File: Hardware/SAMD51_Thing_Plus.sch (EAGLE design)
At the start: 51 parts, among them J6 AMP FCI 10103594-0001LF, Q1 2.5A/30V, U1 MCP73831, U2 ATSAMD51J20A-A, U3 AP2112K-3.3V, U4 4MB Flash, Y1 32.768kHz

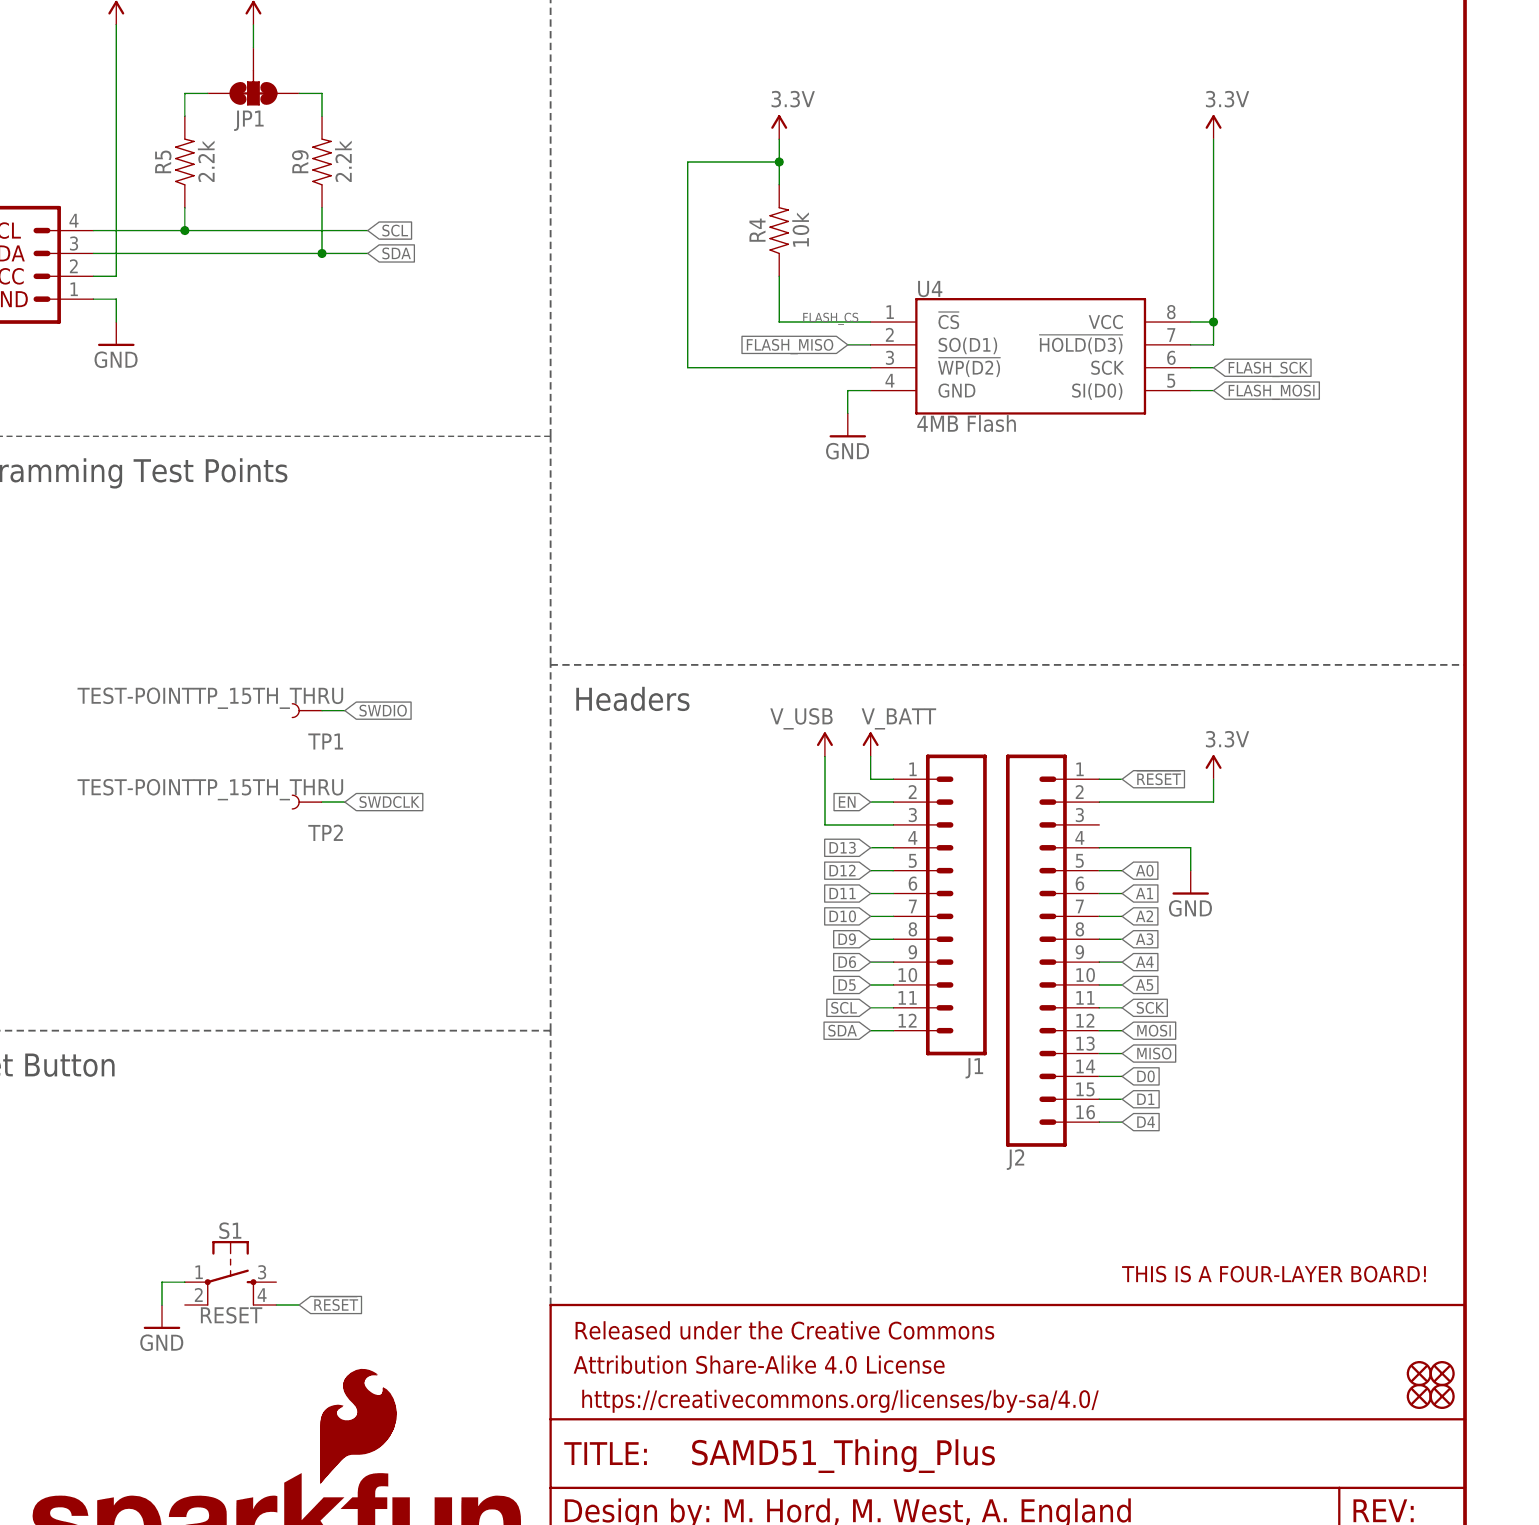
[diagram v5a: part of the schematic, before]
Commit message: adding i2c labels from double check
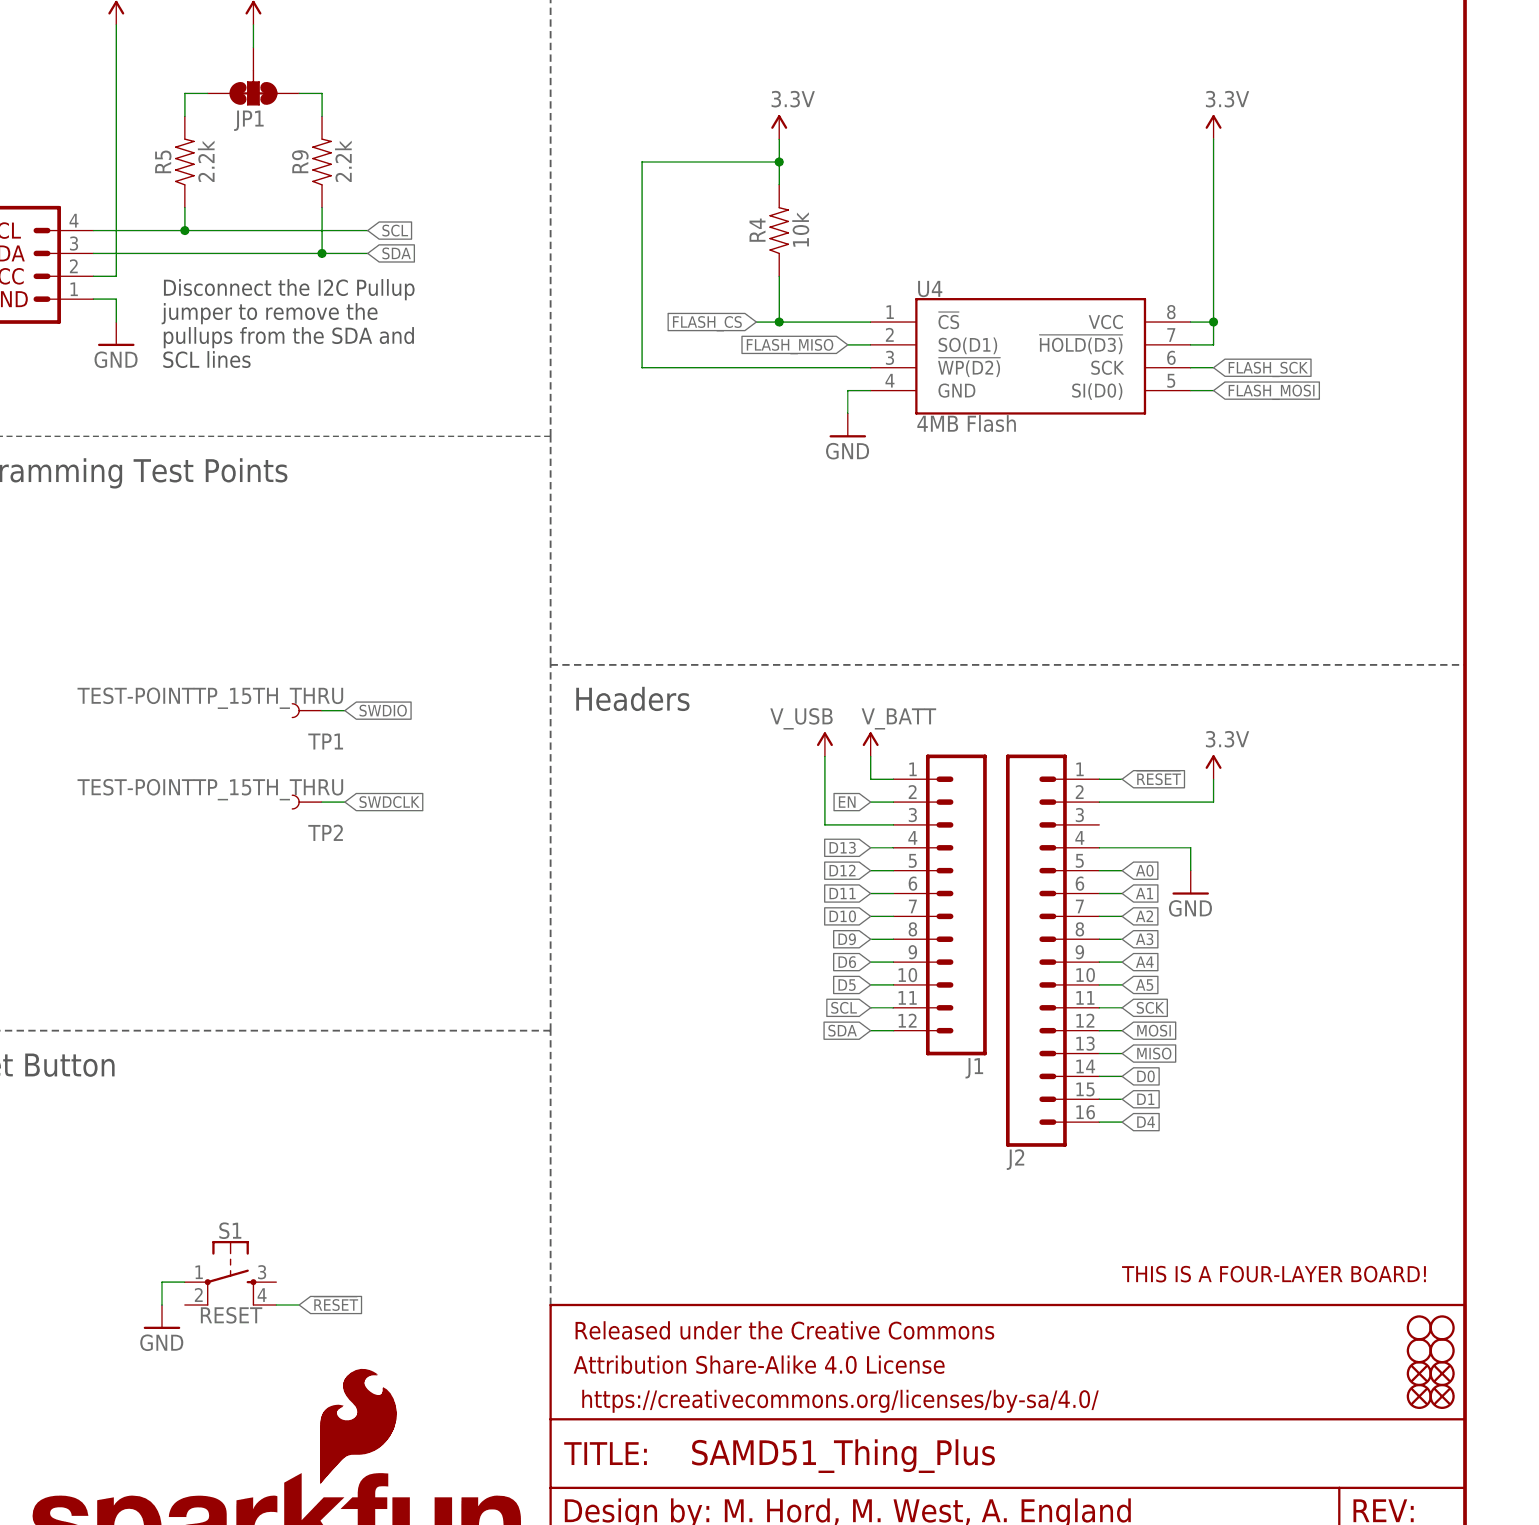
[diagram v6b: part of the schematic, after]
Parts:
- added H1, H2, H3, H4: STAND-OFF, SparkFun-Hardware:STAND-OFF
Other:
- note added: "Disconnect the I2C Pullup jumper to remove the pullups from the SDA and SCL lines"
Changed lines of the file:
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@@
 <part name="JP1" library="SparkFun-Jumpers" deviceset="JUMPER-SMT_3_2-NC_TRACE" device="_SILK"/>
 <part name="SUPPLY15" library="SparkFun-Aesthetics" deviceset="3.3V" device=""/>
+<part name="H1" library="SparkFun-Hardware" deviceset="STAND-OFF" device=""/>
+<part name="H2" library="SparkFun-Hardware" deviceset="STAND-OFF" device=""/>
+<part name="H3" library="SparkFun-Hardware" deviceset="STAND-OFF" device=""/>
+<part name="H4" library="SparkFun-Hardware" deviceset="STAND-OFF" device=""/>
 </parts>
 <sheets>
@@
 <text x="332.74" y="187.96" size="2.54" layer="97" font="vector">Flash Memory</text>
 <wire x1="129.54" y1="193.04" x2="259.08" y2="193.04" width="0.1524" layer="97" style="longdash"/>
+<text x="287.02" y="139.7" size="1.778" layer="97" font="vector">Disconnect the I2C Pullup
+jumper to remove the
+pullups from the SDA and
+SCL lines</text>
 </plain>
 <instances>
@@
 </instance>
 <instance part="SUPPLY15" gate="G$1" x="297.18" y="177.8"/>
+<instance part="H1" gate="G$1" x="426.72" y="30.48"/>
+<instance part="H2" gate="G$1" x="426.72" y="33.02"/>
+<instance part="H3" gate="G$1" x="429.26" y="33.02"/>
+<instance part="H4" gate="G$1" x="429.26" y="30.48"/>
 </instances>
 <busses>
@@
 <pinref part="U4" gate="G$1" pin="!WP(D2)"/>
 <wire x1="355.6" y1="162.56" x2="355.6" y2="165.1" width="0.1524" layer="91"/>
-<wire x1="365.76" y1="139.7" x2="345.44" y2="139.7" width="0.1524" layer="91"/>
-<wire x1="345.44" y1="139.7" x2="345.44" y2="162.56" width="0.1524" layer="91"/>
-<wire x1="345.44" y1="162.56" x2="355.6" y2="162.56" width="0.1524" layer="91"/>
+<wire x1="365.76" y1="139.7" x2="340.36" y2="139.7" width="0.1524" layer="91"/>
+<wire x1="340.36" y1="139.7" x2="340.36" y2="162.56" width="0.1524" layer="91"/>
+<wire x1="340.36" y1="162.56" x2="355.6" y2="162.56" width="0.1524" layer="91"/>
 <junction x="355.6" y="162.56"/>
 </segment>
@@
 <wire x1="355.6" y1="144.78" x2="355.6" y2="149.86" width="0.1524" layer="91"/>
 <pinref part="R4" gate="G$1" pin="1"/>
-<label x="358.14" y="144.78" size="1.016" layer="95" font="vector"/>
-</segment>
-<segment>
+<label x="353.06" y="144.78" size="1.27" layer="95" font="vector" rot="R180" xref="yes"/>
+<wire x1="355.6" y1="144.78" x2="353.06" y2="144.78" width="0.1524" layer="91"/>
+<junction x="355.6" y="144.78"/>
+</segment>
+<segment>

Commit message: pre-design review changes
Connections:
- net D1: now also U2.PA12; no longer U2.PA14
- net FLASH_MOSI: now also U2.PA08; no longer U2.PA09
- net FLASH_SCK: now also U2.PA09; no longer U2.PA08
- net SCK: now also U2.PB13; no longer U2.PA12
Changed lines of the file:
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@@
 </segment>
 <segment>
-<pinref part="U2" gate="G$1" pin="PA08"/>
-<wire x1="93.98" y1="124.46" x2="91.44" y2="124.46" width="0.1524" layer="91"/>
-<label x="91.44" y="124.46" size="1.27" layer="95" font="vector" rot="R180" xref="yes"/>
+<pinref part="U2" gate="G$1" pin="PA09"/>
+<wire x1="93.98" y1="121.92" x2="91.44" y2="121.92" width="0.1524" layer="91"/>
+<label x="91.44" y="121.92" size="1.27" layer="95" font="vector" rot="R180" xref="yes"/>
 </segment>
 </net>
@@
 </segment>
 <segment>
-<pinref part="U2" gate="G$1" pin="PA09"/>
-<wire x1="93.98" y1="121.92" x2="91.44" y2="121.92" width="0.1524" layer="91"/>
-<label x="91.44" y="121.92" size="1.27" layer="95" font="vector" rot="R180" xref="yes"/>
+<pinref part="U2" gate="G$1" pin="PA08"/>
+<wire x1="93.98" y1="124.46" x2="91.44" y2="124.46" width="0.1524" layer="91"/>
+<label x="91.44" y="124.46" size="1.27" layer="95" font="vector" rot="R180" xref="yes"/>
 </segment>
 </net>
@@
 </segment>
 <segment>
+<pinref part="U2" gate="G$1" pin="PB13"/>
+<wire x1="152.4" y1="111.76" x2="154.94" y2="111.76" width="0.1524" layer="91"/>
+<label x="154.94" y="111.76" size="1.27" layer="95" xref="yes"/>
+</segment>
+</net>
+<net name="MOSI" class="0">
+<segment>
+<pinref part="J2" gate="G$1" pin="12"/>
+<wire x1="391.16" y1="66.04" x2="393.7" y2="66.04" width="0.1524" layer="91"/>
+<label x="393.7" y="66.04" size="1.27" layer="95" font="vector" xref="yes"/>
+</segment>
+<segment>
+<pinref part="U2" gate="G$1" pin="PB12"/>
+<wire x1="152.4" y1="114.3" x2="154.94" y2="114.3" width="0.1524" layer="91"/>
+<label x="154.94" y="114.3" size="1.27" layer="95" font="vector" xref="yes"/>
+</segment>
+</net>
+<net name="MISO" class="0">
+<segment>
+<pinref part="J2" gate="G$1" pin="13"/>
+<wire x1="391.16" y1="63.5" x2="393.7" y2="63.5" width="0.1524" layer="91"/>
+<label x="393.7" y="63.5" size="1.27" layer="95" font="vector" xref="yes"/>
+</segment>
+<segment>
+<pinref part="U2" gate="G$1" pin="PB11"/>
+<wire x1="152.4" y1="116.84" x2="154.94" y2="116.84" width="0.1524" layer="91"/>
+<label x="154.94" y="116.84" size="1.27" layer="95" font="vector" xref="yes"/>
+</segment>
+</net>
+<net name="D0" class="0">
+<segment>
+<pinref part="J2" gate="G$1" pin="14"/>
+<wire x1="391.16" y1="60.96" x2="393.7" y2="60.96" width="0.1524" layer="91"/>
+<label x="393.7" y="60.96" size="1.27" layer="95" font="vector" xref="yes"/>
+</segment>
+<segment>
+<pinref part="U2" gate="G$1" pin="PA13"/>
+<wire x1="93.98" y1="111.76" x2="91.44" y2="111.76" width="0.1524" layer="91"/>
+<label x="91.44" y="111.76" size="1.27" layer="95" font="vector" rot="R180" xref="yes"/>
+</segment>
+</net>
+<net name="D1" class="0">
+<segment>
+<pinref part="J2" gate="G$1" pin="15"/>
+<wire x1="391.16" y1="58.42" x2="393.7" y2="58.42" width="0.1524" layer="91"/>
+<label x="393.7" y="58.42" size="1.27" layer="95" font="vector" xref="yes"/>
+</segment>
+<segment>
 <pinref part="U2" gate="G$1" pin="PA12"/>
 <wire x1="93.98" y1="114.3" x2="91.44" y2="114.3" width="0.1524" layer="91"/>
@@
 </segment>
 </net>
-<net name="MOSI" class="0">
-<segment>
-<pinref part="J2" gate="G$1" pin="12"/>
-<wire x1="391.16" y1="66.04" x2="393.7" y2="66.04" width="0.1524" layer="91"/>
-<label x="393.7" y="66.04" size="1.27" layer="95" font="vector" xref="yes"/>
-</segment>
-<segment>
-<pinref part="U2" gate="G$1" pin="PB12"/>
-<wire x1="152.4" y1="114.3" x2="154.94" y2="114.3" width="0.1524" layer="91"/>
-<label x="154.94" y="114.3" size="1.27" layer="95" font="vector" xref="yes"/>
-</segment>
-</net>
-<net name="MISO" class="0">
-<segment>
-<pinref part="J2" gate="G$1" pin="13"/>
-<wire x1="391.16" y1="63.5" x2="393.7" y2="63.5" width="0.1524" layer="91"/>
-<label x="393.7" y="63.5" size="1.27" layer="95" font="vector" xref="yes"/>
-</segment>
-<segment>
-<pinref part="U2" gate="G$1" pin="PB11"/>
-<wire x1="152.4" y1="116.84" x2="154.94" y2="116.84" width="0.1524" layer="91"/>
-<label x="154.94" y="116.84" size="1.27" layer="95" font="vector" xref="yes"/>
-</segment>
-</net>
-<net name="D0" class="0">
-<segment>
-<pinref part="J2" gate="G$1" pin="14"/>
-<wire x1="391.16" y1="60.96" x2="393.7" y2="60.96" width="0.1524" layer="91"/>
-<label x="393.7" y="60.96" size="1.27" layer="95" font="vector" xref="yes"/>
-</segment>
-<segment>
-<pinref part="U2" gate="G$1" pin="PA13"/>
-<wire x1="93.98" y1="111.76" x2="91.44" y2="111.76" width="0.1524" layer="91"/>
-<label x="91.44" y="111.76" size="1.27" layer="95" font="vector" rot="R180" xref="yes"/>
-</segment>
-</net>
-<net name="D1" class="0">
-<segment>
-<pinref part="J2" gate="G$1" pin="15"/>
-<wire x1="391.16" y1="58.42" x2="393.7" y2="58.42" width="0.1524" layer="91"/>
-<label x="393.7" y="58.42" size="1.27" layer="95" font="vector" xref="yes"/>
-</segment>
-<segment>
-<pinref part="U2" gate="G$1" pin="PA14"/>
-<wire x1="93.98" y1="109.22" x2="91.44" y2="109.22" width="0.1524" layer="91"/>
-<label x="91.44" y="109.22" size="1.27" layer="95" font="vector" rot="R180" xref="yes"/>
-</segment>
-</net>
